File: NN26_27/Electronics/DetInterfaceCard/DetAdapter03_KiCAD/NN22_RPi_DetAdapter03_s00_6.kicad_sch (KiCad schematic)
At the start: 54 parts, among them U10 RP2040, U11 MCP1755_DFN, U12 MCP1755_DFN, U13 ADP7142_WSON, U14 ADP7182_WSON, U15 ADP7182_WSON

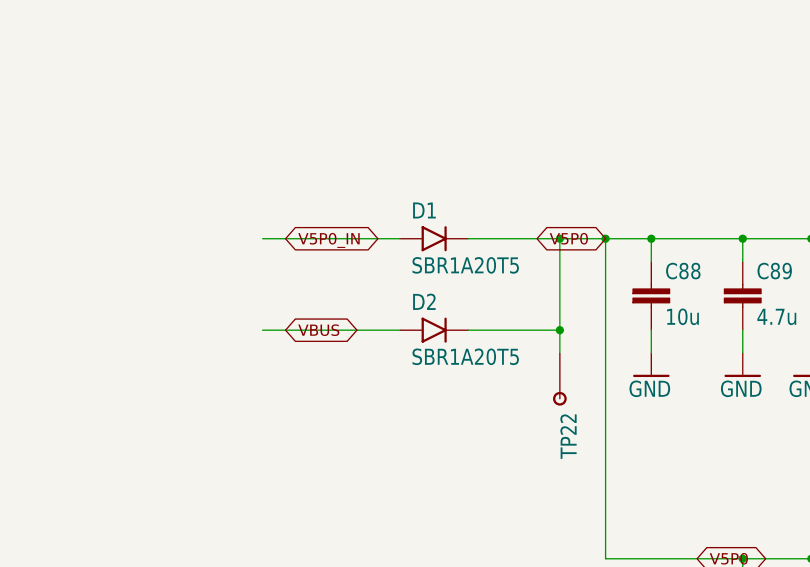
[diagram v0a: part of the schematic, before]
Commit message: change diode footprint
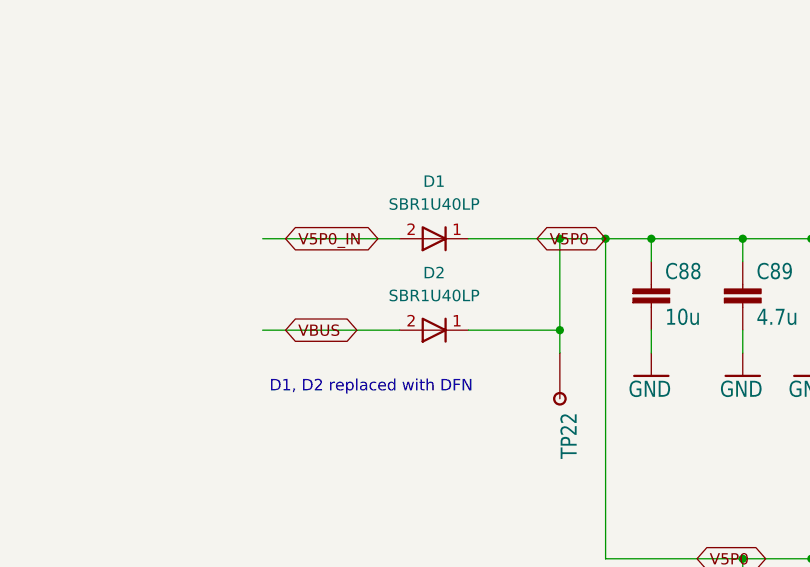
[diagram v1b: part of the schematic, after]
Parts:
- removed D1, D2: SBR1A20T5, NN22_RPi_DetAdapter03_s00:SOD523, symbol NN22_RPi_DetAdapter03_s00-eagle-import:DIODE_SOD523
- added D1, D2: SBR1U40LP, my_DFN:DFN1411, symbol my_Diode:Diode_DFN-3
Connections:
- net V5P0: now also D1.1 (K), D2.1 (K)
- net V5P0_IN: now also D1.2 (A), D1.3 (A)
- net VBUS: now also D2.2 (A), D2.3 (A)
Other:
- note added: "D1, D2 replaced with DFN"

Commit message: update schematic to include MPN1, MFG1
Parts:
- C100, C101, C102, C103, C96, C97, C98, C99: MFG1 (none) -> Murata; MPN1 (none) -> GRM155R71H104KE14D
- C104, C106, C108, C109, C88: MFG1 (none) -> Murata; MPN1 (none) -> GRM188R6YA106MA73D
- C105, C107, C111, C112, C113, C89, C90, C91, C92, C93, C94, C95: MFG1 (none) -> Samsung; MPN1 (none) -> CL05A475MP5NRNC
- C110: MFG1 (none) -> Murata; MPN1 (none) -> GCM155R71E333KA55D
- D1, D2: MFG1 (none) -> Diodes Incorporated; MPN1 (none) -> SBR1U40LP-7
- FID1, FID2, FID3, FID4, FID5, FID6, FID7, FID8, TP17, TP18, TP19, TP20, TP21, TP22: now not fitted
- R65: MFG1 (none) -> Vishay; MPN1 (none) -> CRCW040233R0FKEDC
- R66: MFG1 (none) -> Yageo; MPN1 (none) -> RC0402FR-0730KL
- R67: MFG1 (none) -> Yageo; MPN1 (none) -> RC0402FR-07100KL
- R68, R70: MFG1 (none) -> Yageo; MPN1 (none) -> RC0402FR-1310KL
- R69: MFG1 (none) -> Yageo; MPN1 (none) -> RC0402FR-07154KL
- U10: MFG1 (none) -> Raspberry Pi; MPN1 (none) -> SC0914(7)
- U11, U12: MFG1 (none) -> Microchip; MPN1 (none) -> MCP1755-3302E/MC
- U13: MFG1 (none) -> Analog Devices; MPN1 (none) -> ADP7142ACPZN5.0-R7
- U14, U15: MFG1 (none) -> Analog Devices; MPN1 (none) -> ADP7182ACPZN-R7
